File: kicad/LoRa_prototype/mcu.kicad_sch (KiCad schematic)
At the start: 55 parts, among them J14 SPI_FLASH, J18 MCO, J6 I2C1, J9 UART1, SW1 NRST, U10 STM32WL54CCUx, U8 W25Q16JVSS, X1 LSE, X2 NT2016SF

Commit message: Schematic & footprint assignment done (Milestone)
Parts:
- added FB1: 600@100MHz, Inductor_SMD:L_0603_1608Metric, symbol Device:FerriteBead
- NT1: footprint (none) -> NetTie:NetTie-3_SMD_Pad2.0mm
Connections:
- net VDD: now also FB1.1
- net VDDA: now also FB1.2
- net VDDRF1V55: now also NT1.1; no longer NT1.3
- net VFBSMPS: now also NT1.3; no longer NT1.1

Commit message: Started PCB Layout (Milestone)
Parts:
- D4: footprint PESD3V3L4UG:DIO_PESD3V3L4UG -> footprints:DIO_PESD3V3L4UG
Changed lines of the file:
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@@
 			)
 		)
-		(property "Footprint" "PESD3V3L4UG:DIO_PESD3V3L4UG"
+		(property "Footprint" "footprints:DIO_PESD3V3L4UG"
 			(at 24.13 26.67 0)
 			(hide yes)

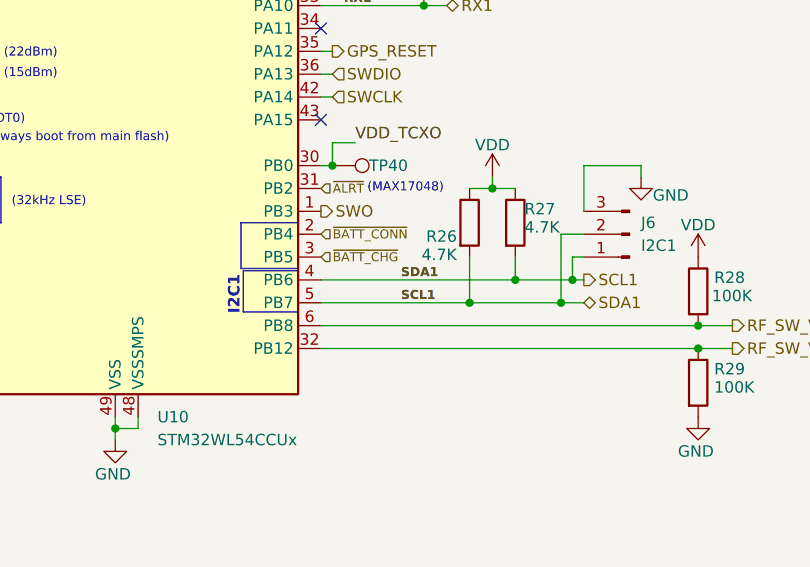
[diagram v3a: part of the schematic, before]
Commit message: Done routing gas sensors
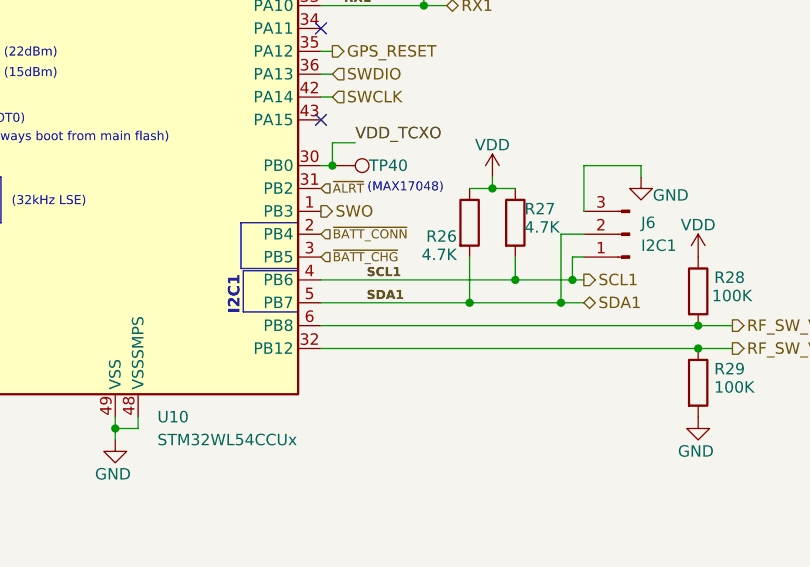
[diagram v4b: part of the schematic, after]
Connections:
- net SCL1: no longer D4.1, J6.2 (Pin_2), R26.2, U10.5 (PB7)
- new net SDA1: D4.1, J6.2 (Pin_2), R26.2, U10.5 (PB7)
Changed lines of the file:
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@@
 	)
 	(label "SCL1"
-		(at 133.35 138.43 0)
+		(at 129.54 135.89 0)
 		(effects
 			(font
@@
 	)
 	(label "SDA1"
-		(at 133.35 135.89 0)
+		(at 129.54 138.43 0)
 		(effects
 			(font

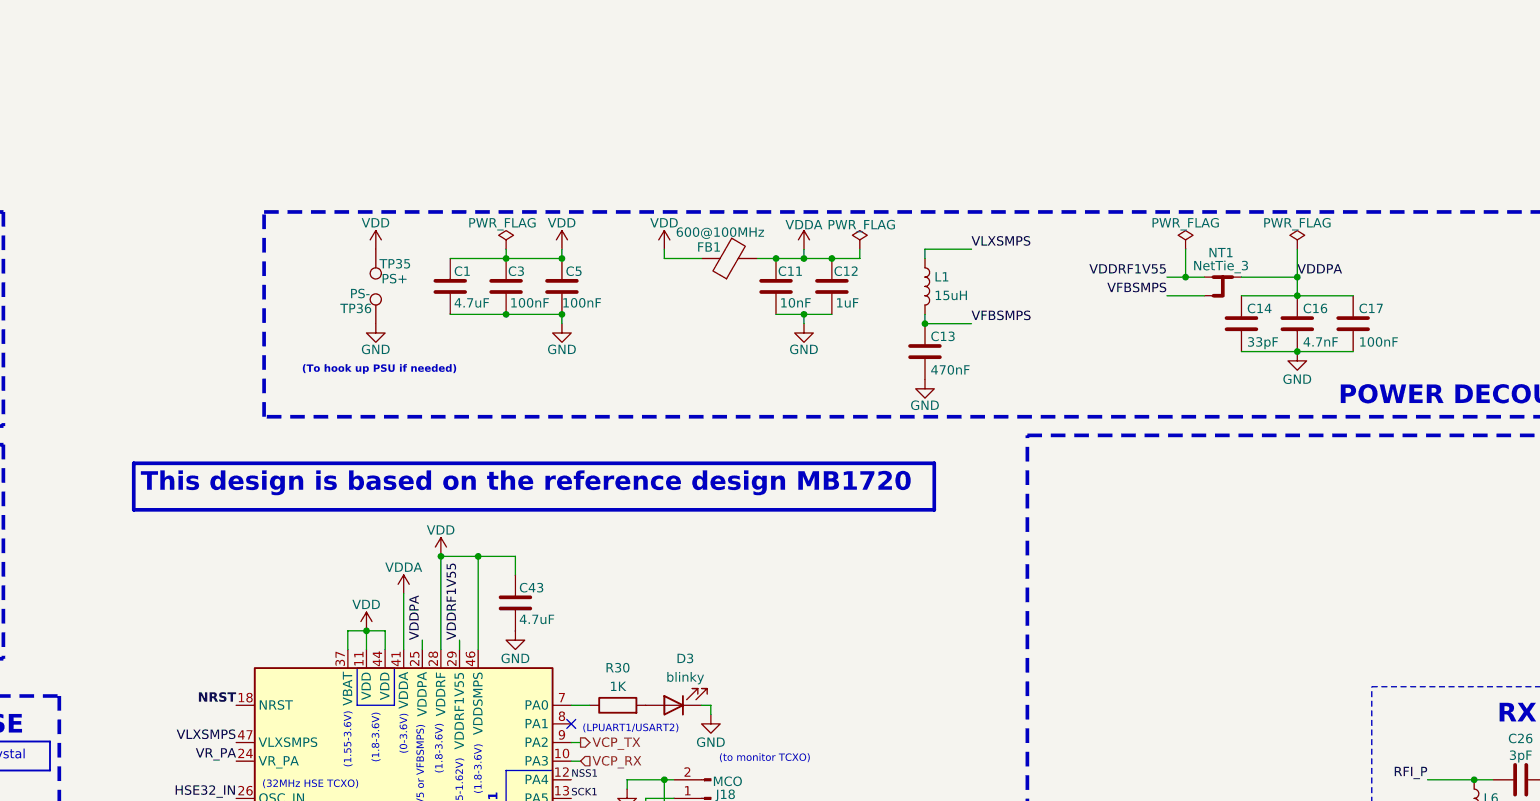
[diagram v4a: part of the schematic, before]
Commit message: Changed decoupling in schematic
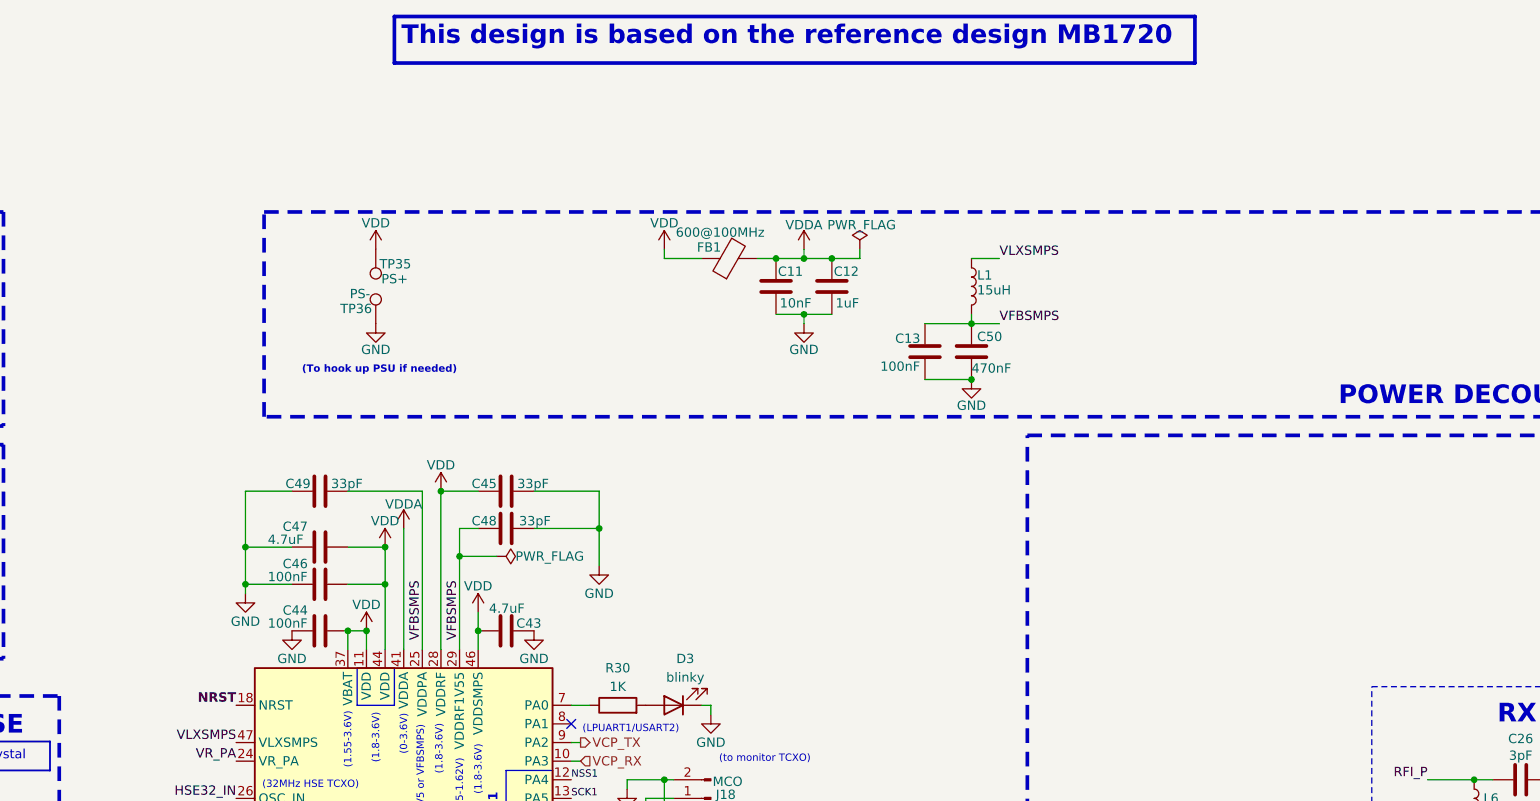
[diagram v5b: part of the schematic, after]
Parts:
- removed C1: 4.7uF, Capacitor_SMD:C_0805_2012Metric, symbol Device:C
- removed C14: 33pF, Capacitor_SMD:C_0402_1005Metric, symbol Device:C
- removed C16: 4.7nF, Capacitor_SMD:C_0805_2012Metric, symbol Device:C
- removed C17, C3, C5: 100nF, Capacitor_SMD:C_0805_2012Metric, symbol Device:C
- removed NT1: NetTie_3, NetTie:NetTie-3_SMD_Pad2.0mm, symbol Device:NetTie_3
- added C44, C46, C50: 100nF, Capacitor_SMD:C_0402_1005Metric, symbol Device:C
- added C45, C48, C49: 33pF, Capacitor_SMD:C_0402_1005Metric, symbol Device:C
- added C47: 4.7uF, Capacitor_SMD:C_0402_1005Metric, symbol Device:C
- C11, C12, C13, C18, C19, C2, C23, C42, C43, C6, C9: footprint Capacitor_SMD:C_0805_2012Metric -> Capacitor_SMD:C_0402_1005Metric
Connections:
- net VDDPA is gone; now on net VFBSMPS: U10.25 (VDDPA)
- net VDDRF1V55 is gone; now on net VFBSMPS: U10.29 (VDDRF1V55)
- net GND: now also C44.2, C45.2, C46.2, C47.2, C48.2, C49.1, C50.2
- net VDD: now also C44.1, C45.1, C46.1, C47.1
- net VFBSMPS: now also C48.1, C49.2, C50.1
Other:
- moved on the sheet: C43, L1

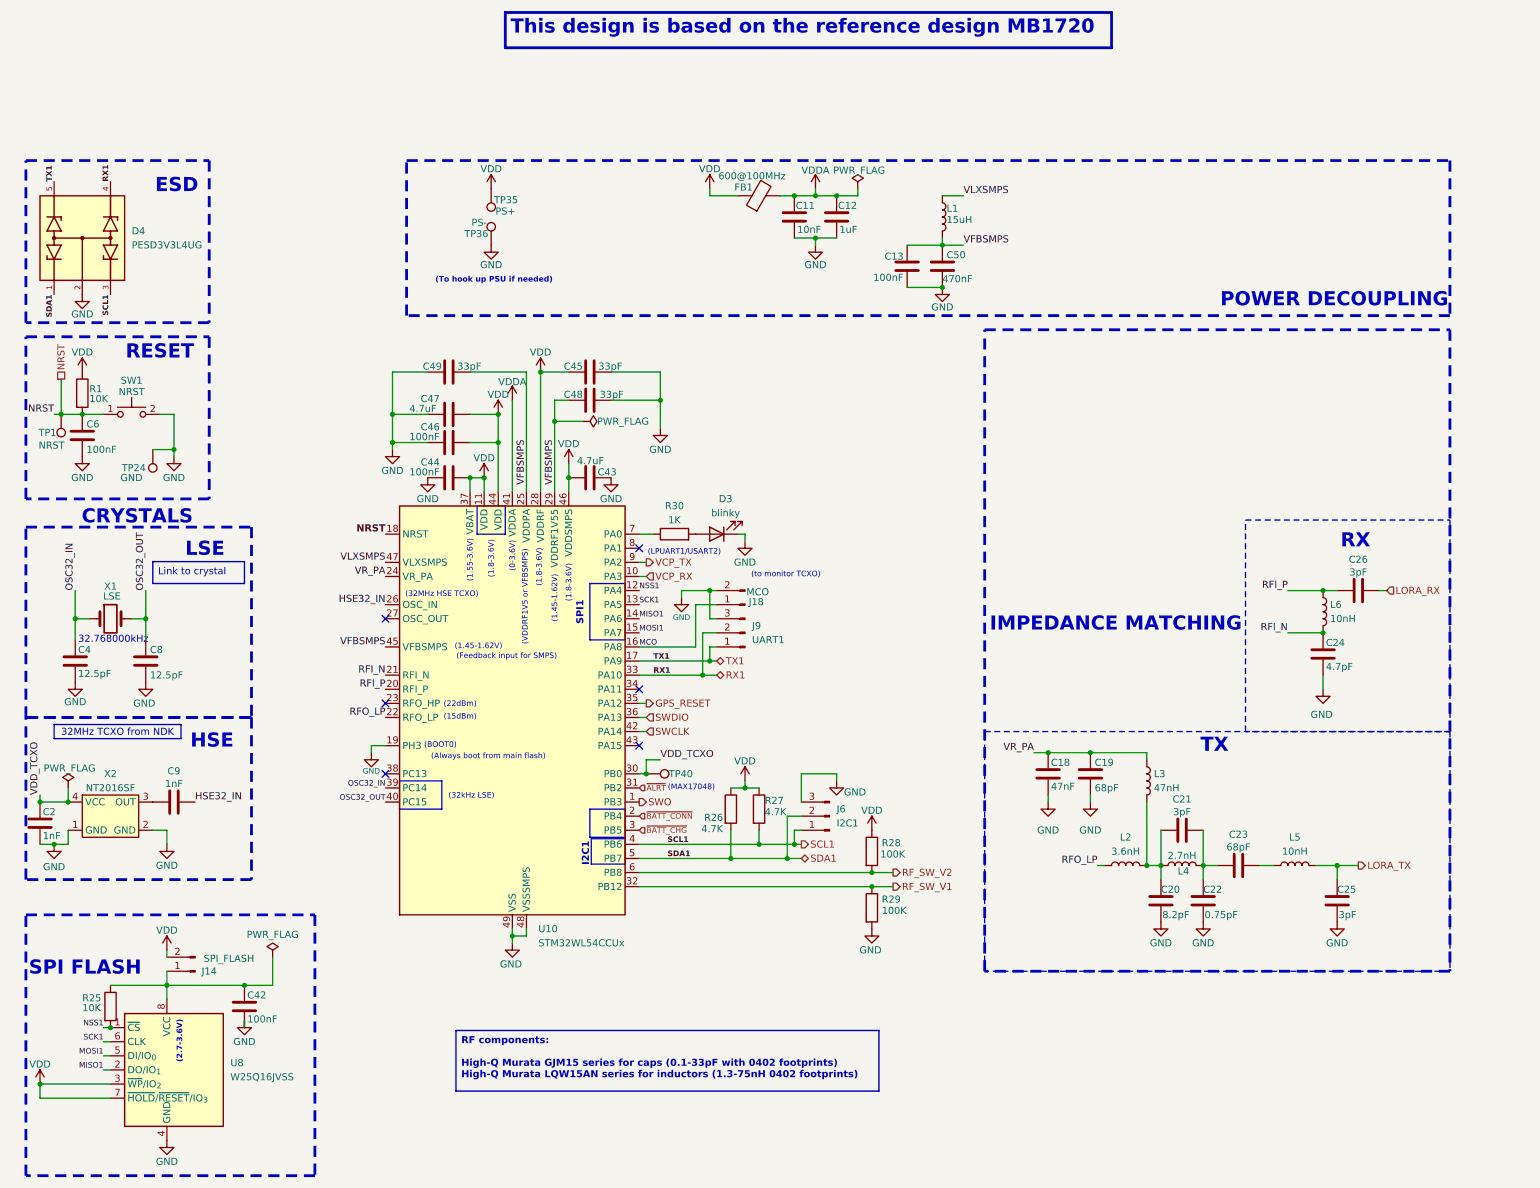
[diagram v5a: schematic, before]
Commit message: Cleaned up schematic
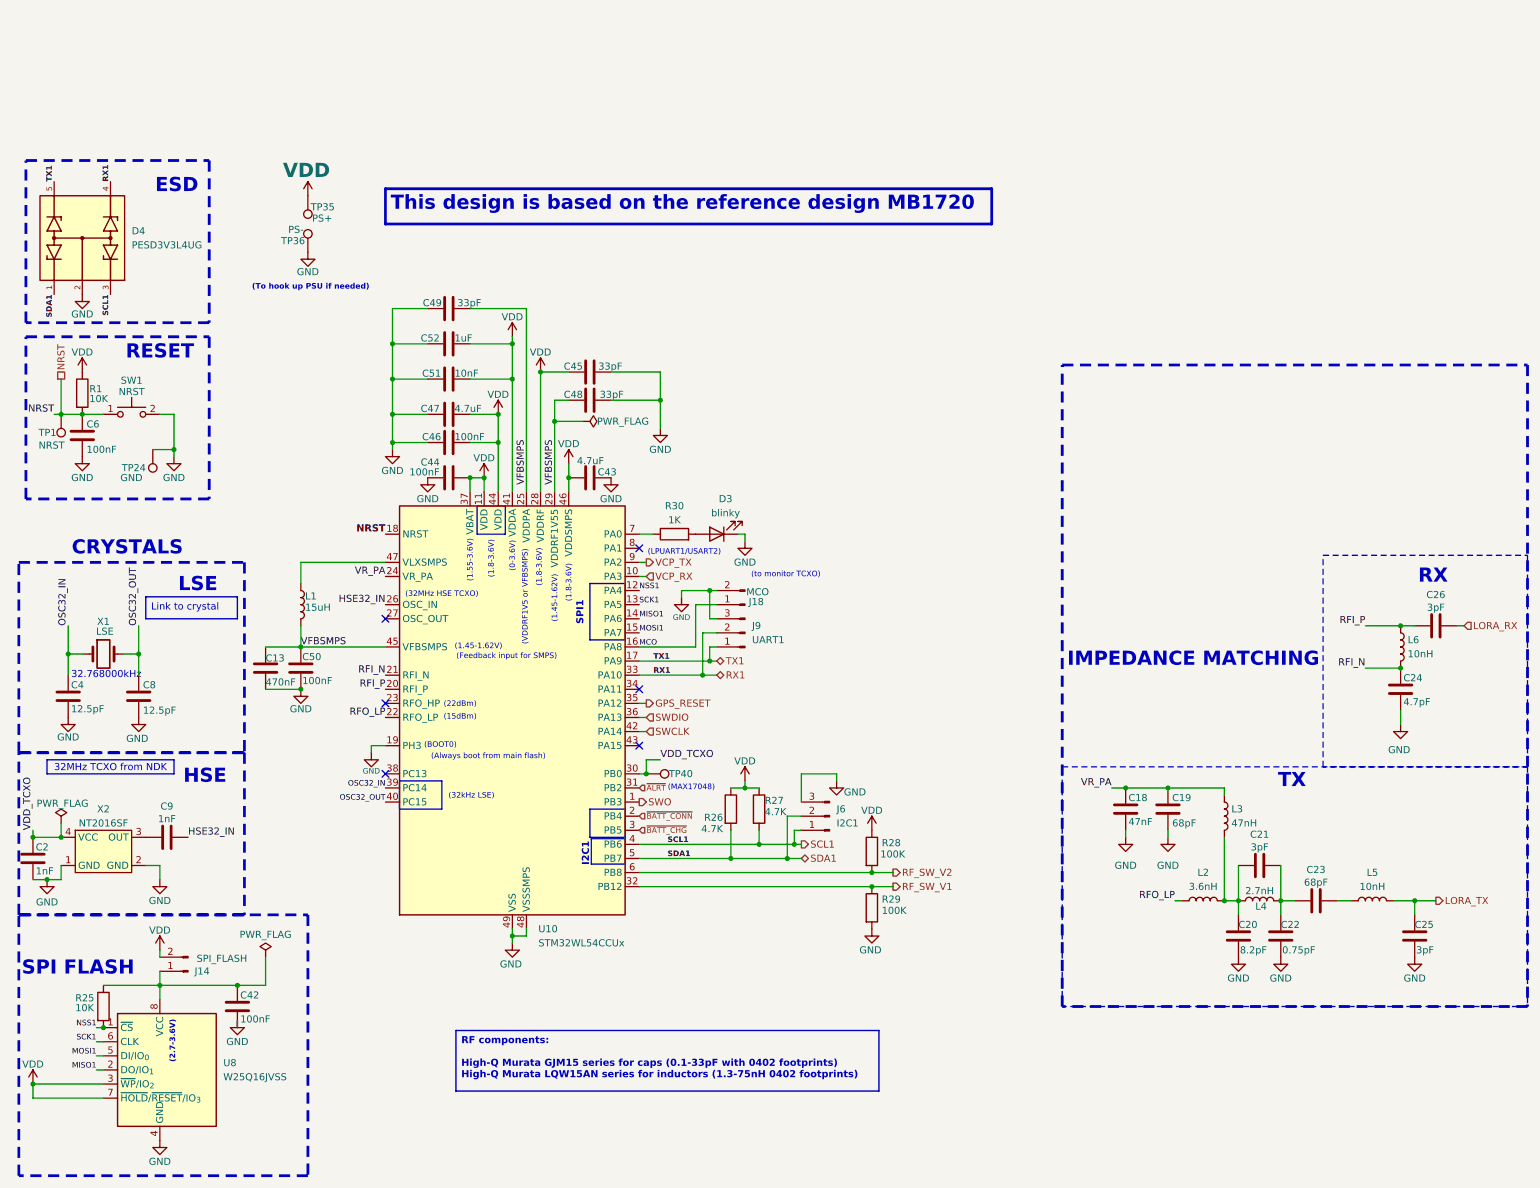
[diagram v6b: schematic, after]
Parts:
- removed C11: 10nF, Capacitor_SMD:C_0402_1005Metric, symbol Device:C
- removed C12: 1uF, Capacitor_SMD:C_0402_1005Metric, symbol Device:C
- removed FB1: 600@100MHz, Inductor_SMD:L_0603_1608Metric, symbol Device:FerriteBead
- added C51: 10nF, Capacitor_SMD:C_0402_1005Metric, symbol Device:C
- added C52: 1uF, Capacitor_SMD:C_0402_1005Metric, symbol Device:C
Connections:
- net VDDA is gone; now on net VDD: U10.41 (VDDA)
- net GND: now also C51.2, C52.2
- net VDD: now also C51.1, C52.1
- net VLXSMPS: no longer names the net of L1.1, U10.47 (VLXSMPS)
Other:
- note removed: "POWER DECOUPLING"
- moved on the sheet: C13, C18, C19, C2, C20, C21, C22, C23, C24, C25, C26, C4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

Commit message: Routed I2C and ESD protection for MCU
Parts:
- R26, R27, R28, R29, R30: footprint Resistor_SMD:R_0805_2012Metric -> Resistor_SMD:R_0603_1608Metric
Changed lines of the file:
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@@
 			)
 		)
-		(property "Footprint" "Resistor_SMD:R_0805_2012Metric"
+		(property "Footprint" "Resistor_SMD:R_0603_1608Metric"
 			(at 130.81 81.788 90)
 			(hide yes)
@@
 			)
 		)
-		(property "Footprint" "Resistor_SMD:R_0805_2012Metric"
+		(property "Footprint" "Resistor_SMD:R_0603_1608Metric"
 			(at 164.592 137.16 90)
 			(hide yes)
@@
 			)
 		)
-		(property "Footprint" "Resistor_SMD:R_0805_2012Metric"
+		(property "Footprint" "Resistor_SMD:R_0603_1608Metric"
 			(at 144.272 129.54 90)
 			(hide yes)
@@
 			)
 		)
-		(property "Footprint" "Resistor_SMD:R_0805_2012Metric"
+		(property "Footprint" "Resistor_SMD:R_0603_1608Metric"
 			(at 139.192 129.54 90)
 			(hide yes)
@@
 			)
 		)
-		(property "Footprint" "Resistor_SMD:R_0805_2012Metric"
+		(property "Footprint" "Resistor_SMD:R_0603_1608Metric"
 			(at 164.592 147.32 90)
 			(hide yes)

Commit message: Done routing antenna and RF switch
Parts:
- R1: footprint Resistor_SMD:R_0805_2012Metric -> Resistor_SMD:R_0603_1608Metric
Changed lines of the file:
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@@
 			)
 		)
-		(property "Footprint" "Resistor_SMD:R_0805_2012Metric"
+		(property "Footprint" "Resistor_SMD:R_0603_1608Metric"
 			(at 22.352 54.61 90)
 			(hide yes)
